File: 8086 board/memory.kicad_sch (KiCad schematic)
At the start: 44 parts, among them U10 74AC573, U11 74AC573, U12 74AC573, U13 29F800BA, U14 IS61C6416AL, U2 74HC32, U20 74HC138, U21 74HC138, U25 IS61C6416AL

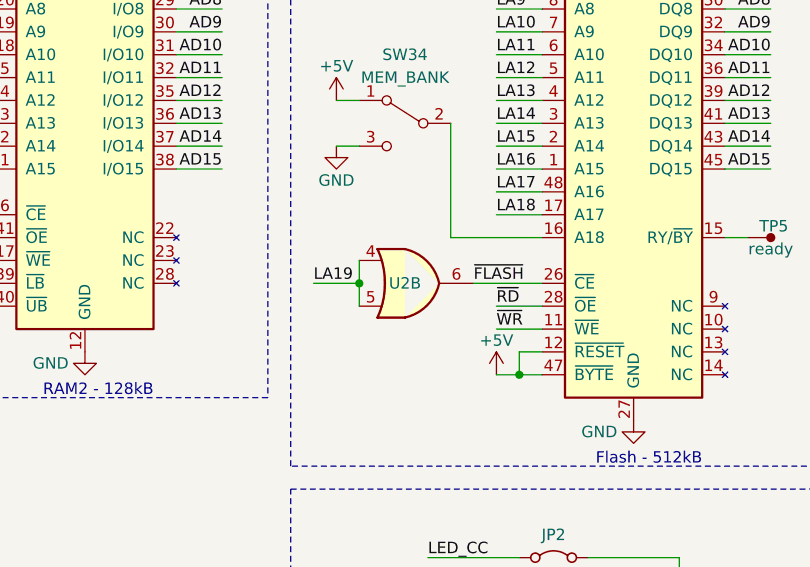
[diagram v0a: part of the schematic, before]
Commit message: PCB: move to kicad 8
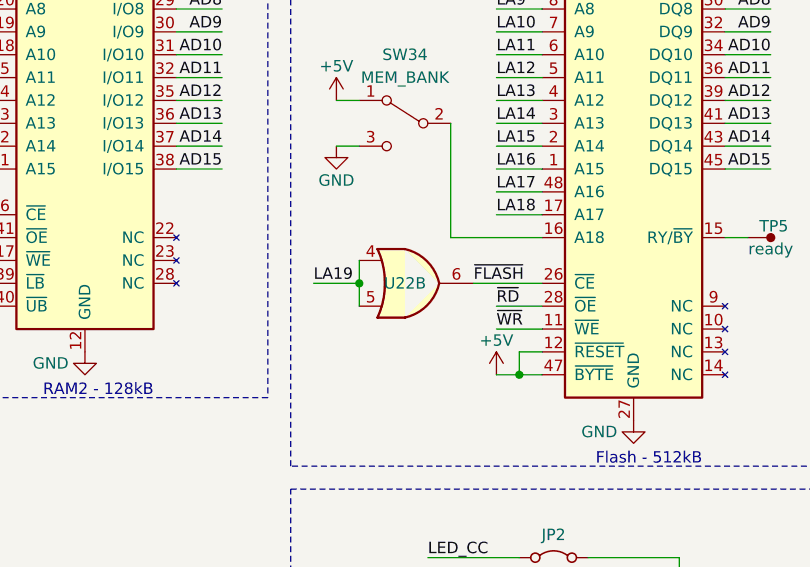
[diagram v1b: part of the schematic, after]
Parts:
- renumbered U2 to U22
